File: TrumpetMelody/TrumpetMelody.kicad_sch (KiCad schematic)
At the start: 11 parts, among them SW1 SW_Push, U1 STM32F411RETx

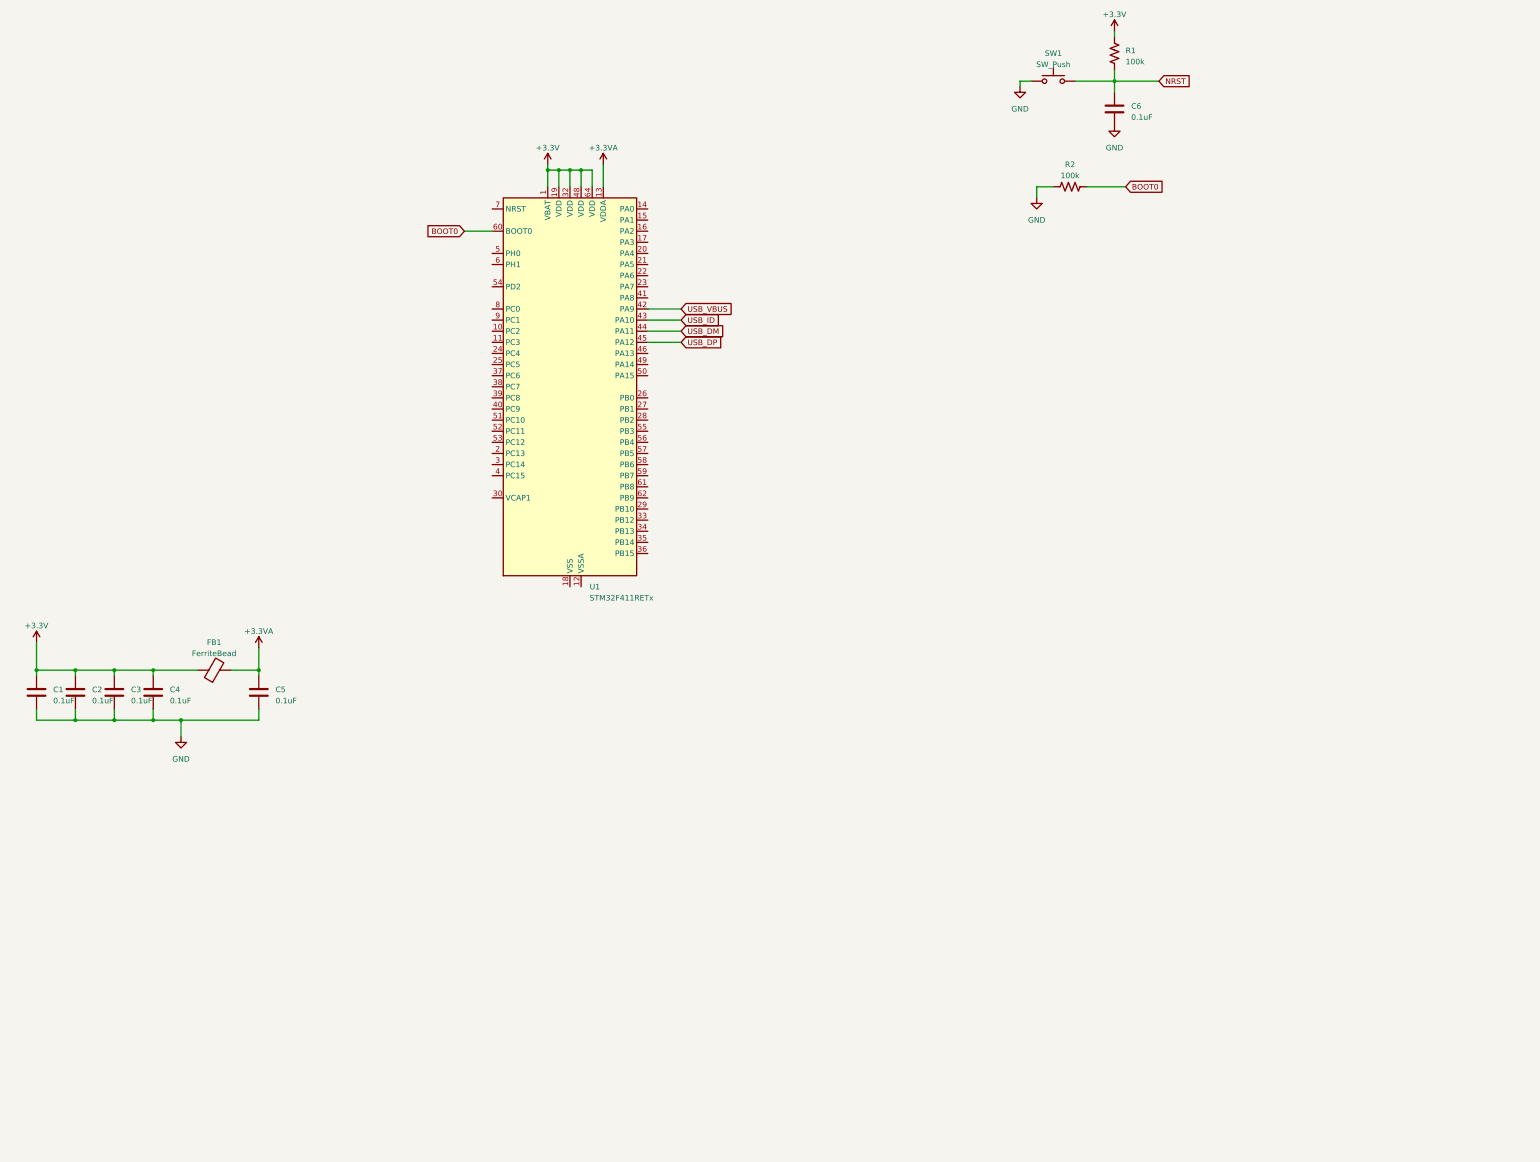
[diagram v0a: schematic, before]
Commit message: Started Design and imported some schematics
Manually created and scoped out the switching regulator
Set areas for different parts
Started work on speakers by importing MAX98357 symbol and creating a project library
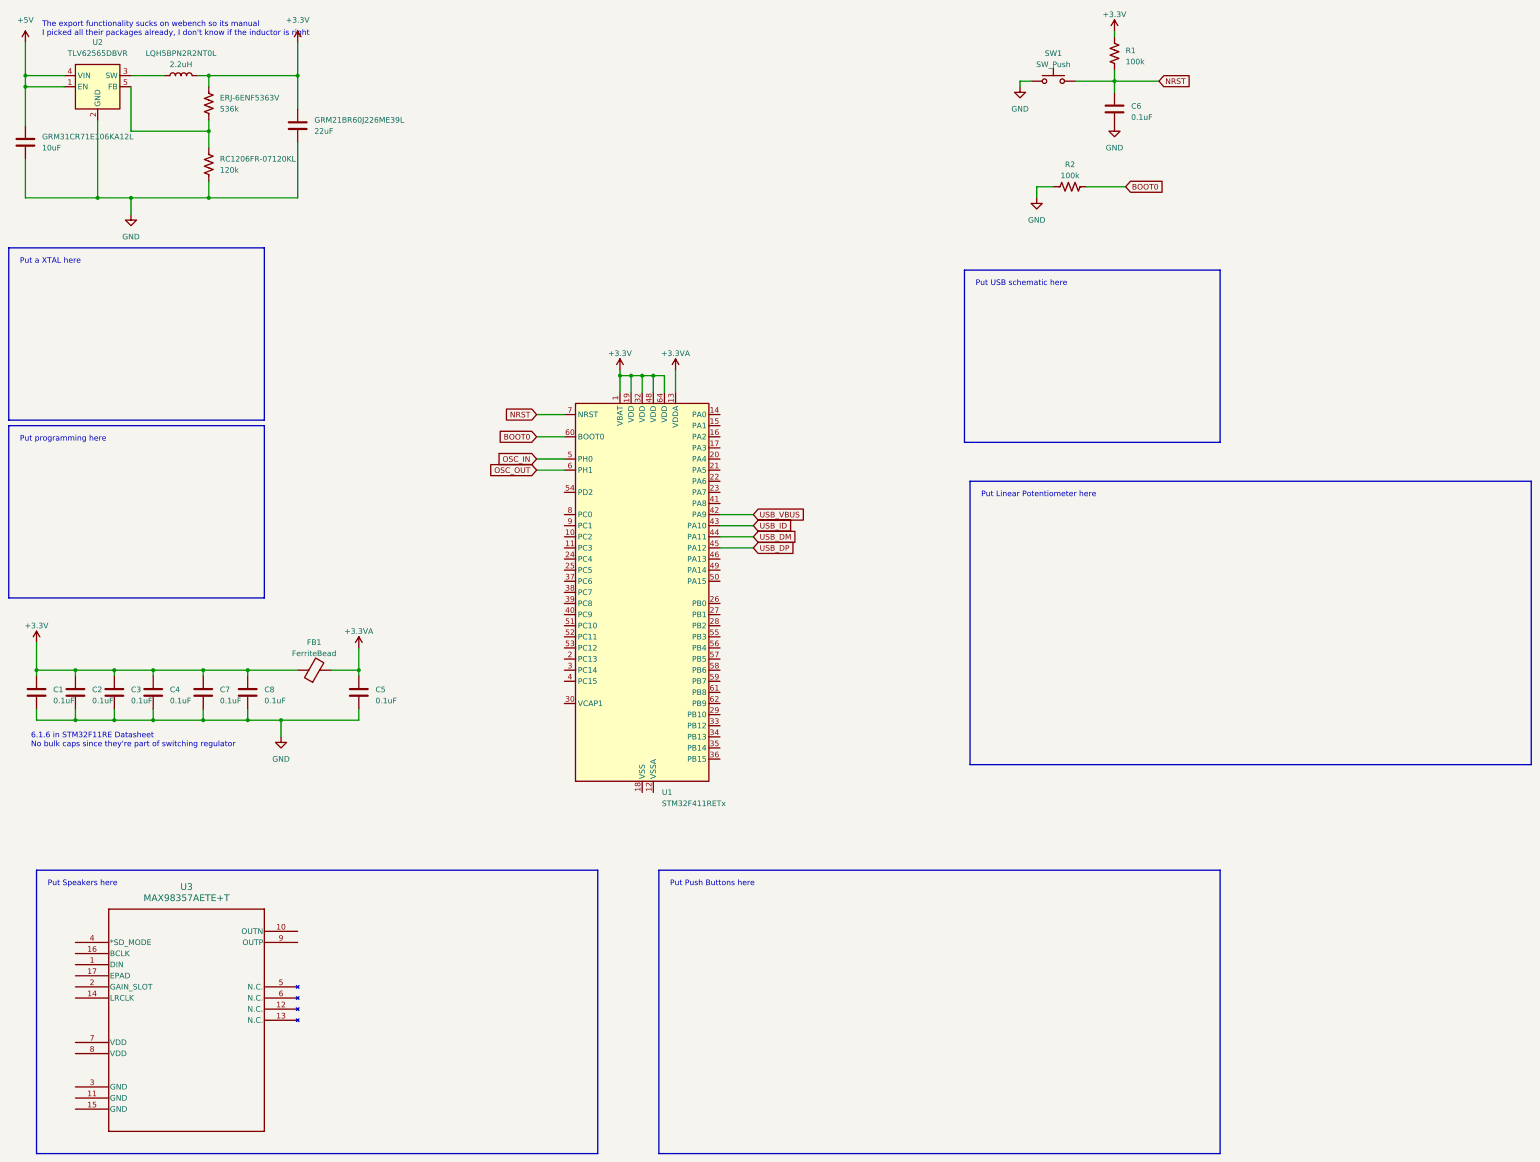
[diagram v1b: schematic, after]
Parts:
- added C7, C8: 0.1uF, symbol Device:C
- added ERJ-6ENF5363V: 536k, Resistor_SMD:R_0805_2012Metric_Pad1.20x1.40mm_HandSolder, symbol Device:R_US
- added GRM21BR60J226ME39L: 22uF, Capacitor_SMD:C_0805_2012Metric_Pad1.18x1.45mm_HandSolder, symbol Device:C
- added GRM31CR71E106KA12L: 10uF, Capacitor_SMD:C_1206_3216Metric_Pad1.33x1.80mm_HandSolder, symbol Device:C
- added LQH5BPN2R2NT0L: 2.2uH, Inductor_SMD:L_Murata_LQH55DN_5.7x5.0mm, symbol Device:L
- added RC1206FR-07120KL: 120k, Resistor_SMD:R_1206_3216Metric_Pad1.30x1.75mm_HandSolder, symbol Device:R_US
- added U2: TLV62565DBVR, Package_TO_SOT_SMD:SOT-23-5_HandSoldering, symbol Regulator_Switching:TLV62568DBV
- added U3: MAX98357AETE+T, 21-0136I_T1633-4_MXM, symbol TrumpetMelody_Symbol_Library:MAX98357AETE+T
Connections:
- net +3.3V: now also C7.1, C8.1, ERJ-6ENF5363V.1, GRM21BR60J226ME39L.1, LQH5BPN2R2NT0L.2
- net GND: now also C7.2, C8.2, GRM21BR60J226ME39L.2, GRM31CR71E106KA12L.2, RC1206FR-07120KL.2, U2.2 (GND)
- net NRST: now also U1.7 (NRST)
- net OSC_IN: now reaches U1.5 (PH0)
- net OSC_OUT: now reaches U1.6 (PH1)
- new net: LQH5BPN2R2NT0L.1, U2.3 (SW)
- new net: ERJ-6ENF5363V.2, RC1206FR-07120KL.1, U2.5 (FB)
- new net +5V: GRM31CR71E106KA12L.1, U2.1 (EN), U2.4 (VIN)
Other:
- note added: "6.1.6 in STM32F11RE Datasheet No bulk caps since they're part of switching regulator"
- note added: "Put Linear Potentiometer here"
- note added: "Put Push Buttons here"
- note added: "Put Speakers here"
- note added: "Put USB schematic here"
- note added: "Put a XTAL here"
- note added: "Put programming here"
- note added: "The export functionality sucks on webench so its manual I picked all their packages already, I don't know if the inductor is right"
- moved on the sheet: C5, FB1, U1

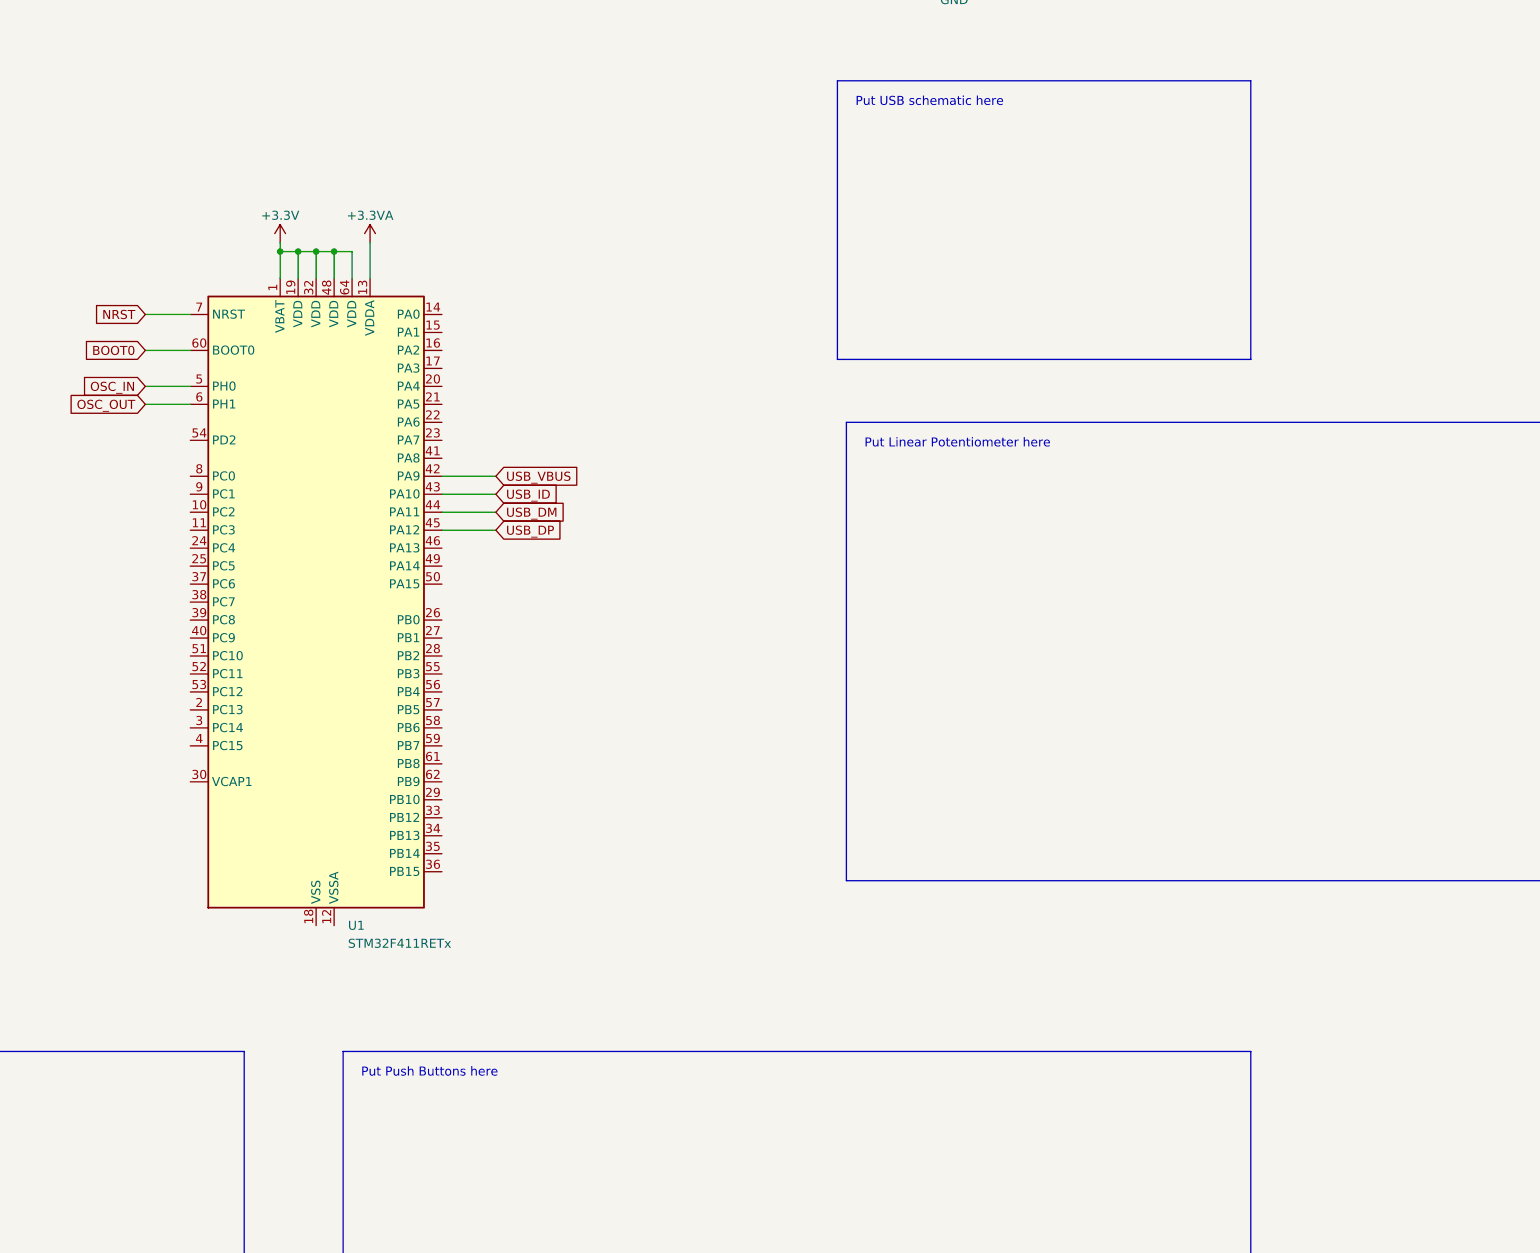
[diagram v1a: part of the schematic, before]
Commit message: To CLAYTON: Marked some details out for the different components
Please try to do the things that would be easier for you to do and harder for me to do.
I.E. USB schem, XTAL schem, marking pins with labels, putting those labels in their corresponding boxes too, programming header.
I can handle doing the peripherals after getting past pin assignments, I will also try to add some debugging things now, but mostly that will be done during layout.
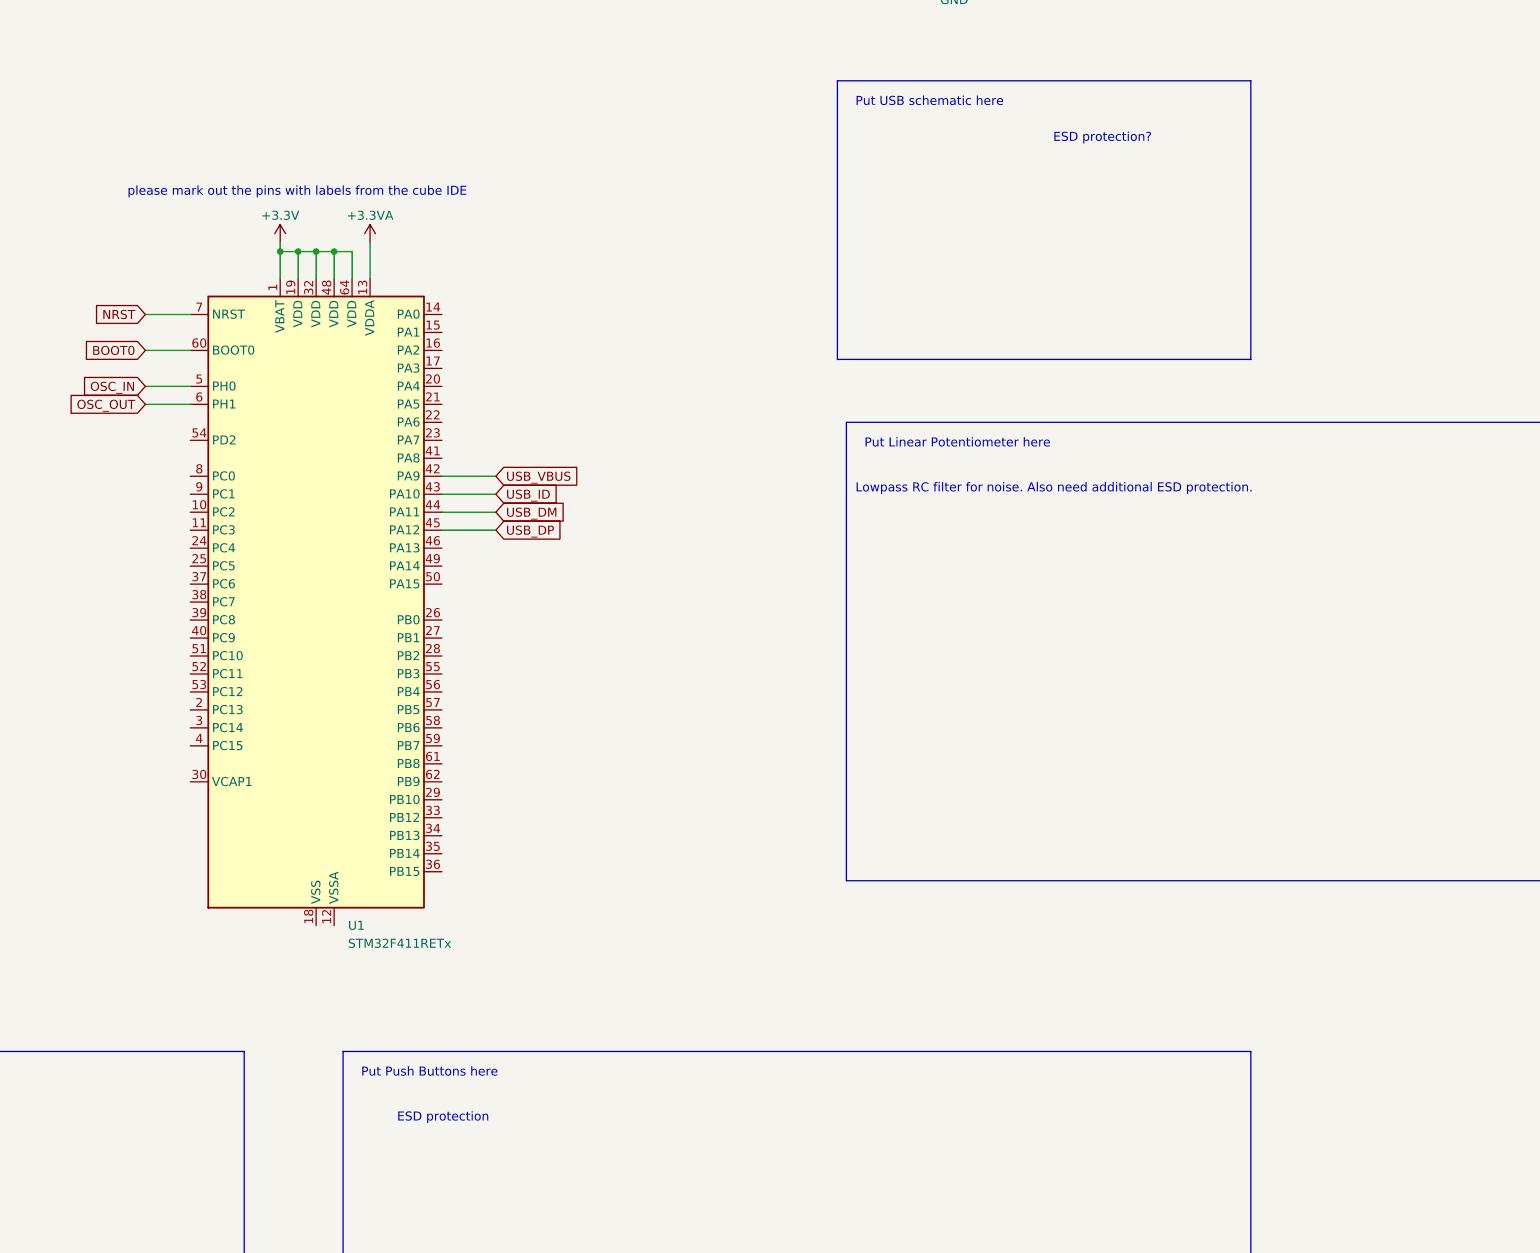
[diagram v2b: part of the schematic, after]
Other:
- note added: "ESD protection"
- note added: "ESD protection?"
- note added: "Lowpass RC filter for noise. Also need additional ESD protection."
- note added: "please mark out the pins with labels from the cube IDE"
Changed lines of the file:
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@@
+    (effects (font (size 1.27 1.27)) (justify left bottom))
+  )
+  (text "ESD protection" (at 167.64 219.71 0)
     (effects (font (size 1.27 1.27)) (justify left bottom))
   )
@@
     (effects (font (size 1.27 1.27)) (justify left bottom))
   )
+  (text "ESD protection?" (at 260.35 81.28 0)
+    (effects (font (size 1.27 1.27)) (justify left bottom))
+  )
   (text "Put programming here" (at 13.97 111.76 0)
     (effects (font (size 1.27 1.27)) (justify left bottom))
@@
     (effects (font (size 1.27 1.27)) (justify left bottom))
   )
+  (text "please mark out the pins with labels from the cube IDE"
+    (at 129.54 88.9 0)
+    (effects (font (size 1.27 1.27)) (justify left bottom))
+  )
+  (text "Lowpass RC filter for noise. Also need additional ESD protection."
+    (at 232.41 130.81 0)
+    (effects (font (size 1.27 1.27)) (justify left bottom))
+  )
